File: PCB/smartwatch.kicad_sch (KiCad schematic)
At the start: 16 parts, among them J1 Conn_01x04_Pin, SW1 SW_Push, U1 STM32L432KBUx, U2 LSM6DS3, U3 W25Q128JVPIQ, U4 TP4056, X1 SG-5032CAN, Y2 LSE 32khz

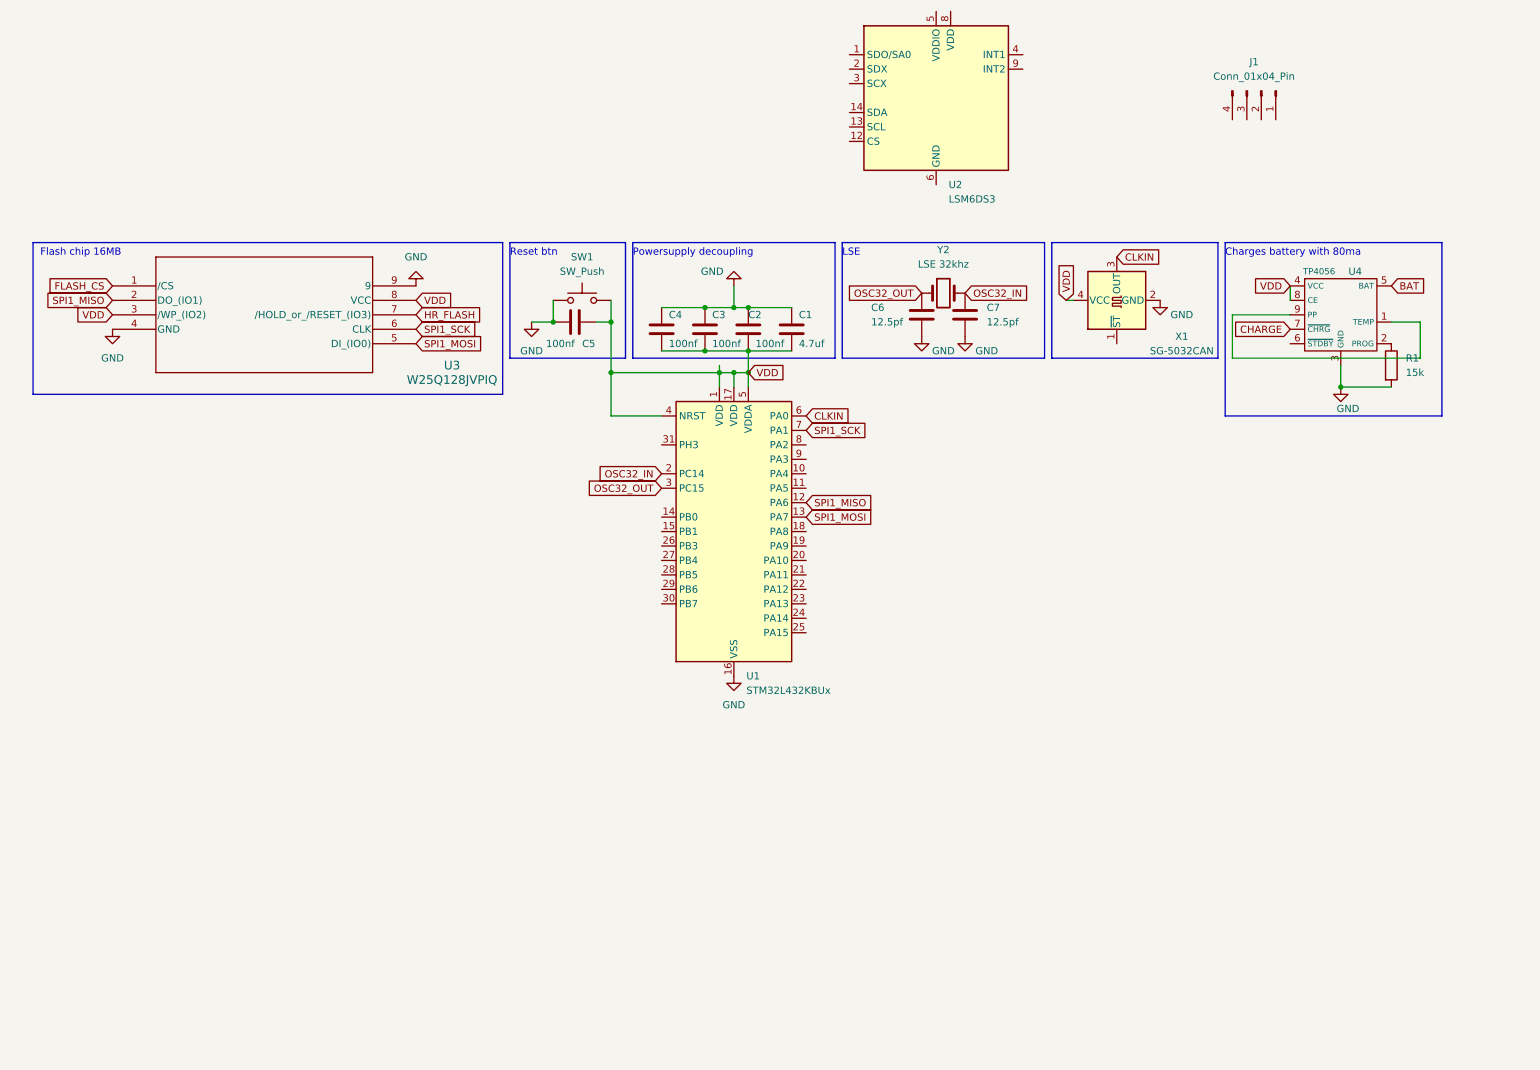
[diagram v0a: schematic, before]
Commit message: Added gyroscope
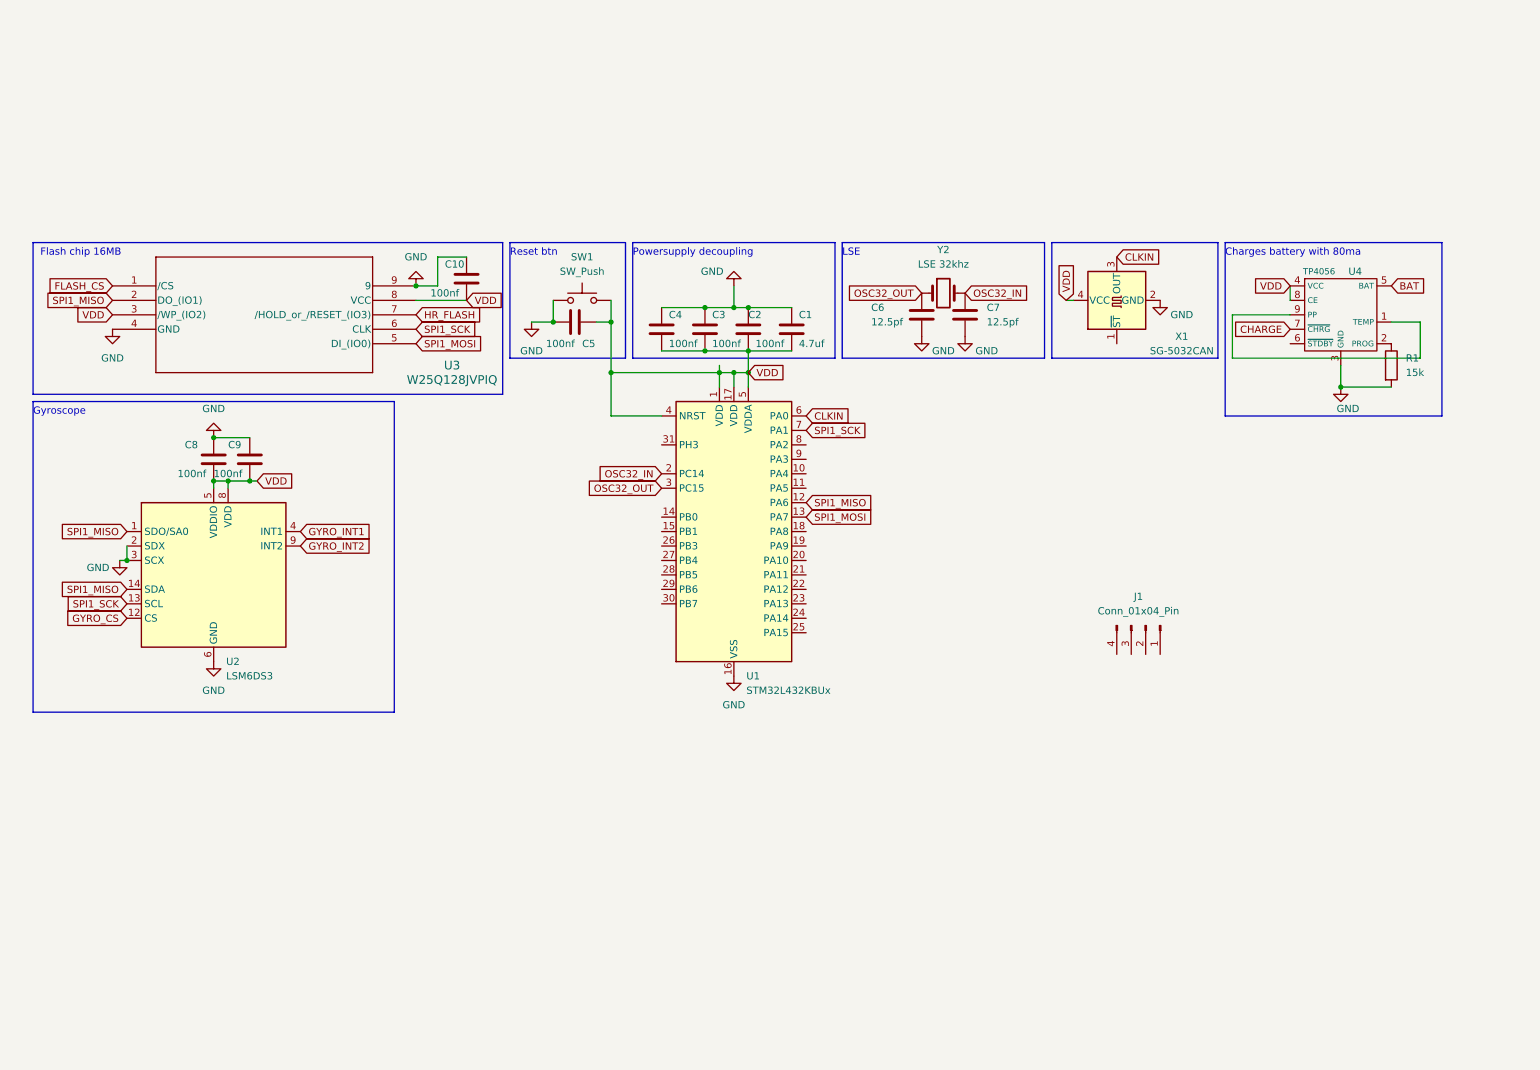
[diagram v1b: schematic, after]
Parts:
- added C10, C8, C9: 100nf, symbol Device:C
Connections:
- net GND: now also U2.2 (SDX), U2.3 (SCX), U2.6 (GND), U2.7 (GND), C10.1, C8.1, C9.1
- net SPI1_MISO: now also U2.1 (SDO/SA0), U2.14 (SDA)
- net SPI1_SCK: now also U2.13 (SCL)
- net VDD: now also U2.5 (VDDIO), U2.8 (VDD), C10.2, C8.2, C9.2
- net GYRO_CS: now reaches U2.12 (CS)
- net GYRO_INT1: now reaches U2.4 (INT1)
- net GYRO_INT2: now reaches U2.9 (INT2)
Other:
- note added: "Gyroscope"
- moved on the sheet: J1, U2

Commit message: new staffz
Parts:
- removed X1: SG-5032CAN, Oscillator:Oscillator_SMD_SeikoEpson_SG8002LB-4Pin_5.0x3.2mm, symbol Oscillator:SG-5032CAN
- added C11, C12, C13: 4.7uf, Capacitor_SMD:C_0603_1608Metric, symbol Device:C
- added J2: Battery input, symbol Connector_Generic:Conn_01x02
- added U5: LT1761-3.3, Package_TO_SOT_SMD:TSOT-23-5, symbol Regulator_Linear:LT1761-3.3
- added X2: 20Mhz, Crystal:Crystal_SMD_3225-4Pin_3.2x2.5mm, symbol Oscillator:ASCO
- C1, C10, C2, C3, C4, C5, C8, C9: footprint (none) -> Capacitor_SMD:C_0603_1608Metric
- C6, C7: value 12.5pf -> 9pf; footprint (none) -> Capacitor_SMD:C_0603_1608Metric
- J1: value Conn_01x04_Pin -> Serial wire/Charging
- Y2: footprint (none) -> Crystal:Crystal_SMD_3215-2Pin_3.2x1.5mm
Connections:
- net BAT: now also C11.2, C12.1, J2.2 (Pin_2), U5.1 (VIN), U5.3 (~{SHDN})
- net CLKIN: now also X2.3 (OUT)
- net GND: now also J1.4 (Pin_4), U4.1 (TEMP), U4.9 (PP), C11.1, C12.2, C13.2, J2.1 (Pin_1), U5.2 (GND), X2.2 (GND)
- net VDD: now also U5.5 (VOUT), X2.1 (Tri-State), X2.4 (VDD); no longer C5.1, SW1.2, U1.4 (NRST), U4.4 (VCC), U4.8 (CE)
- net VIN: now reaches J1.3 (Pin_3)
- net VIN: now also U4.4 (VCC), U4.8 (CE)
- new net: C5.1, SW1.2, U1.4 (NRST)
- new net: C13.1, U5.4 (BYP)
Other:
- note added: "20Mhz clock SX3M20"
- note added: "Battery stuff"
- note added: "LSE DXTF32"
- note added: "TODO LIST: - Buttons - Battery - Serial Wire - Power Supply"
- note removed: "LSE"
- moved on the sheet: J1, R1, U4

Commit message: files?
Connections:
- net BAT: now also U1.7 (PA1)
- net FLASH_CS: now also U1.18 (PA8)
- net GYRO_CS: now also U1.29 (PB6)
- net SPI1_MOSI: no longer U1.13 (PA7)
- net SWCLK: now reaches J1.1 (Pin_1)
- net SWCLK: now also U1.24 (PA14)
- net SWDIO: now reaches J1.2 (Pin_2)
- net SWDIO: now also U1.25 (PA15)
- net FLASH_SCK: now reaches U1.11 (PA5)
- net FLASH_SCK: now also U3.6 (CLK)
- net GYRO_SCK: now reaches U1.26 (PB3)
- net GYRO_SCK: now also U2.13 (SCL)
- net GYRO_MISO: now reaches U1.27 (PB4)
- net GYRO_MISO: now also U2.1 (SDO/SA0)
- net GYRO_MOSI: now reaches U1.28 (PB5)
- net GYRO_MOSI: now also U2.14 (SDA)
- net SPI1_MISO renamed FLASH_MISO
- net FLASH_MISO: no longer U2.1 (SDO/SA0), U2.14 (SDA)
- removed net SPI1_SCK: U1.7 (PA1), U2.13 (SCL), U3.6 (CLK)
- new net FLASH_MOSI: U1.13 (PA7)
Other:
- note added: "TODO LIST: - Buttons"
- note removed: "TODO LIST: - Buttons - Battery - Serial Wire - Power Supply"

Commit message: All but routing done
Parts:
- removed SW1: SW_Push, symbol Switch:SW_Push
- added C14, C15, C16: 100nf, Capacitor_SMD:C_0603_1608Metric, symbol Device:C
- added D1, D2: D, Diode_SMD:D_0201_0603Metric, symbol Device:D
- added J3: Conn_01x15, Connector_FFC-FPC:TE_1-1734839-5_1x15-1MP_P0.5mm_Horizontal, symbol Connector_Generic:Conn_01x15
- added J4: Conn_01x03, Connector_FFC-FPC:TE_0-1734839-5_1x05-1MP_P0.5mm_Horizontal, symbol Connector_Generic:Conn_01x03
- added J5: USB_B_Micro, Connector_USB:USB_Micro-B_Amphenol_10118194_Horizontal, symbol Connector:USB_B_Micro
- added R10, R5, R6, R9: 4.7k, Resistor_SMD:R_0805_2012Metric, symbol Device:R
- added R2, R4: 1R, Resistor_SMD:R_0805_2012Metric, symbol Device:R
- added R3: 10k, Resistor_SMD:R_0805_2012Metric, symbol Device:R
- added R7, R8: [Jumper], Resistor_SMD:R_0805_2012Metric, symbol Device:R
- added SW1: SW_SPDT, MyButtons:MSK12CO2, symbol Switch:SW_SPDT
- added U6: INA3221, Package_DFN_QFN:Texas_RGV0016A_VQFN-16-1EP_4x4mm_P0.65mm_EP2.1x2.1mm, symbol Power_Management:INA3221
- added U8: USBLC6-2SC6, Package_TO_SOT_SMD:SOT-23-6, symbol Power_Protection:USBLC6-2SC6
- J1: footprint Connector_PinHeader_2.54mm:PinHeader_1x04_P2.54mm_Horizontal -> Connector_PinHeader_2.54mm:PinHeader_1x04_P2.54mm_Vertical
- J2: footprint (none) -> Connector_PinHeader_2.54mm:PinHeader_1x02_P2.54mm_Vertical
- R1: footprint (none) -> Resistor_SMD:R_0805_2012Metric
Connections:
- net FLASH_MOSI is gone; now on net GYRO_INT1: U1.13 (PA7)
- net HR_FLASH is gone; now on net VDD: U3.7 (/HOLD_or_/RESET_(IO3))
- net SPI1_MOSI is gone; now on net QUADSPI_IO0: U3.5 (DI_(IO0))
- net BAT: now also SW1.2 (B); no longer U5.1 (VIN), U5.3 (~{SHDN})
- net CHARGE: now also U1.11 (PA5), R10.2
- net GND: now also C5.1, U2.1 (SDO/SA0), C14.2, C15.2, C16.1, J3.1 (Pin_1), J3.11 (Pin_11), J3.2 (Pin_2), J4.2 (Pin_2), J5.4 (ID), J5.5 (GND), J5.6 (Shield), R7.1, U6.17 (EP), U6.3 (GND), U6.5 (A0), U8.2 (GND); no longer C5.2
- net GYRO_INT2: now also U1.27 (PB4)
- net SWDIO: now also U1.23 (PA13); no longer U1.25 (PA15)
- net VDD: now also C5.2, U2.12 (CS), C14.1, J3.10 (Pin_10), J3.4 (Pin_4), J4.3 (Pin_3), R10.1, R3.2, R4.1, R4.2, R5.1, R6.1, R8.1, U6.14 (IN-2), U6.15 (IN+2), U6.16 (VPU), U6.4 (VS)
- net VIN: now also C16.2, D1.1 (K), D2.1 (K); no longer J1.3 (Pin_3)
- net at U1.4 (NRST): no longer C5.1
- net HEARTBEAT_AOUT: now reaches U1.10 (PA4)
- net HEARTBEAT_AOUT: now also C15.1, J4.1 (Pin_1)
- net QUADSPI_IO1: now reaches U1.14 (PB0)
- net QUADSPI_IO1: now also U3.2 (DO_(IO1))
- net QUADSPI_IO0: now reaches U1.15 (PB1)
- net I2C1_SCL: now reaches U1.19 (PA9)
- net I2C1_SCL: now also U2.13 (SCL), J3.15 (Pin_15), R5.2, U6.6 (SCL)
- net I2C1_SDA: now reaches U1.20 (PA10)
- net I2C1_SDA: now also U2.14 (SDA), J3.14 (Pin_14), R6.2, U6.7 (SDA)
- net USB_DM: now reaches U1.21 (PA11)
- net USB_DM: now also U8.4 (I/O2)
- net USB_DP: now reaches U1.22 (PA12)
- net USB_DP: now also U8.6 (I/O1)
- net TP_RST: now reaches U1.30 (PB7)
- net TP_RST: now also J3.12 (Pin_12)
- net at U1.31 (PH3): now also R7.2, R9.2
- net QUADSPI_NCS: now reaches U1.8 (PA2)
- net QUADSPI_NCS: now also U3.1 (/CS)
- net QUADSPI_CLK: now reaches U1.9 (PA3)
- net QUADSPI_CLK: now also U3.6 (CLK)
- net FLASH_CS renamed LCD_RS
- net LCD_RS: now also J3.5 (Pin_5); no longer U3.1 (/CS)
- net FLASH_MISO renamed LEDA
- net LEDA: now also J3.3 (Pin_3); no longer U3.2 (DO_(IO1))
- removed net FLASH_SCK: U1.11 (PA5), U3.6 (CLK)
- net GYRO_CS renamed TP_INT
- net TP_INT: now also J3.13 (Pin_13); no longer U2.12 (CS)
- removed net GYRO_MISO: U1.27 (PB4), U2.1 (SDO/SA0)
- net GYRO_MOSI renamed LCD_MOSI
- net LCD_MOSI: now also J3.8 (Pin_8); no longer U2.14 (SDA)
- net GYRO_SCK renamed LCD_SCK
- net LCD_SCK: now also J3.7 (Pin_7); no longer U2.13 (SCL)
- new net: D2.2 (A), J1.3 (Pin_3)
- new net: R8.2, R9.1
- new net: D1.2 (A), J5.1 (VBUS), U8.5 (VBUS)
- new net: J5.3 (D+), U8.1 (I/O1)
- new net: J5.2 (D-), U8.3 (I/O2)
- new net: R3.1, U6.10 (PV)
- new net BATSHUNTH: R2.1, R2.2, SW1.1 (A), U5.1 (VIN), U5.3 (~{SHDN}), U6.11 (IN-1), U6.12 (IN+1)
- new net LCD_NSS: J3.6 (Pin_6), U1.25 (PA15)
- new net RST: J3.9 (Pin_9)
- no-connect marks 0 -> 7
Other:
- note added: "Cheap Short Protection"
- note added: "Display connector"
- note added: "I2C Address: 00010101b"
- note added: "I2C Address: 1000000b"
- note added: "I2C Address: 1101010b"
- note added: "I2C PULLUPS"
- note added: "Potential Heartbeat connector"
- note removed: "Reset btn"
- note removed: "TODO LIST: - Buttons"
- moved on the sheet: C1, C10, C11, C12, C13, C2, C3, C4, C6, C7, C8, C9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

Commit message: pcb done
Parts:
- removed R8: [Jumper], Resistor_SMD:R_0805_2012Metric, symbol Device:R
- removed R9: 4.7k, Resistor_SMD:R_0805_2012Metric, symbol Device:R
- D1, D2: footprint Diode_SMD:D_0201_0603Metric -> Diode_SMD:D_0603_1608Metric
- J3: footprint Connector_FFC-FPC:TE_1-1734839-5_1x15-1MP_P0.5mm_Horizontal -> MyButtons:FPC-SMD_15P-P0.50_KH-FG0.5-H2.0-15P-SMT
- J4: footprint Connector_FFC-FPC:TE_0-1734839-5_1x05-1MP_P0.5mm_Horizontal -> Connector_PinHeader_2.54mm:PinHeader_1x03_P2.54mm_Vertical
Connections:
- net TP_RST is gone; now on net LCD_RST: J3.12 (Pin_12), U1.30 (PB7)
- net BATSHUNTH: no longer R2.1, SW1.1 (A), U6.11 (IN-1)
- net VDD: no longer C1.2, C2.2, C3.2, C4.2, R4.1, U1.1 (VDD), U1.17 (VDD), U1.5 (VDDA), U6.14 (IN-2)
- net at J5.3 (D+): now also U8.6 (I/O1); no longer U8.1 (I/O1)
- net at J5.2 (D-): now also U8.4 (I/O2); no longer U8.3 (I/O2)
- net RST renamed LCD_RST
- net USB_DM renamed USB_D-
- net USB_D-: now also U8.3 (I/O2); no longer U8.4 (I/O2)
- net USB_DP renamed USB_D+
- net USB_D+: now also U8.1 (I/O1); no longer U8.6 (I/O1)
- new net BATSHUNTL: R2.1, SW1.1 (A), U6.11 (IN-1)
- new net VDDSHUNTL: C1.2, C2.2, C3.2, C4.2, R4.1, U1.1 (VDD), U1.17 (VDD), U1.5 (VDDA), U6.14 (IN-2)
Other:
- note removed: "Cheap Short Protection"
